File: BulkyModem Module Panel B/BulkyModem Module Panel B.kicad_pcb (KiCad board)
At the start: 2 copper layers, 100 x 23.2 mm, 20 parts, among them J1 Front Panel, M1 Mounting_Pin, M2 Mounting_Pin, M3 Mounting_Pin, M4 Mounting_Pin, SW1 MODE, SW2 POW

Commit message: Alternate panel designs
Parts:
- removed JP1: BYPASS, solder_bridge:bridge
- added R2: 2k2, Resistor_THT:R_Axial_DIN0207_L6.3mm_D2.5mm_P10.16mm_Horizontal, F.Cu at (132.2, 115.2)
- D17: value POW -> LED_RGBC; footprint LED_THT:LED_D5.0mm -> LED_THT:LED_D5.0mm-4_RGB_Wide_Pins
- R1: value 470 -> 3k3
- moved R1 38.7 mm to (117.6, 115.2)
- moved D4 19.7 mm to (148.7, 115.2), turned to 0 degrees
- moved D3 11.4 mm to (144.3, 115.2), turned to 180 degrees
- moved D17 3.32 mm to (96.7, 122.6), turned to 0 degrees
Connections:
- D17 pad 1: /LED_POW -> Net-(D17-Pad1)
- D3 pad 1: Net-(D17-Pad2) -> Net-(D3-Pad1)
- D4 pad 1: Net-(D17-Pad2) -> Net-(D3-Pad1)
- D4 pad 2: Net-(D4-Pad2) -> VSB
- J1 pad 3: /LED_POW -> (no net)
- R1 pad 1: VSB -> Net-(D3-Pad1)
- R1 pad 2: Net-(D4-Pad2) -> Net-(D17-Pad1)
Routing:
- net Net-(D3-Pad1): track 0.00 -> 35.2 mm
- net Net-(D4-Pad2): track 26.1 -> 0.00 mm
- net /LED_POW: track 24.8 -> 0.00 mm
- net VSB: track 24.8 -> 48.0 mm
- net Net-(D17-Pad1): track 0.00 -> 17.0 mm
- net Net-(D17-Pad2): track 41.6 -> 29.2 mm
- net VCC: track 119.8 -> 125.6 mm, vias 1 -> 0
- net /LED_C64: track 20.4 -> 18.8 mm
- net SW_PWR: track 23.0 -> 23.5 mm
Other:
- board text added: "BulkyModem Module Panel B (rev. A) github.com/tebl"
- board text removed: "BulkyModem Module Panel (rev. B) github.com/tebl"

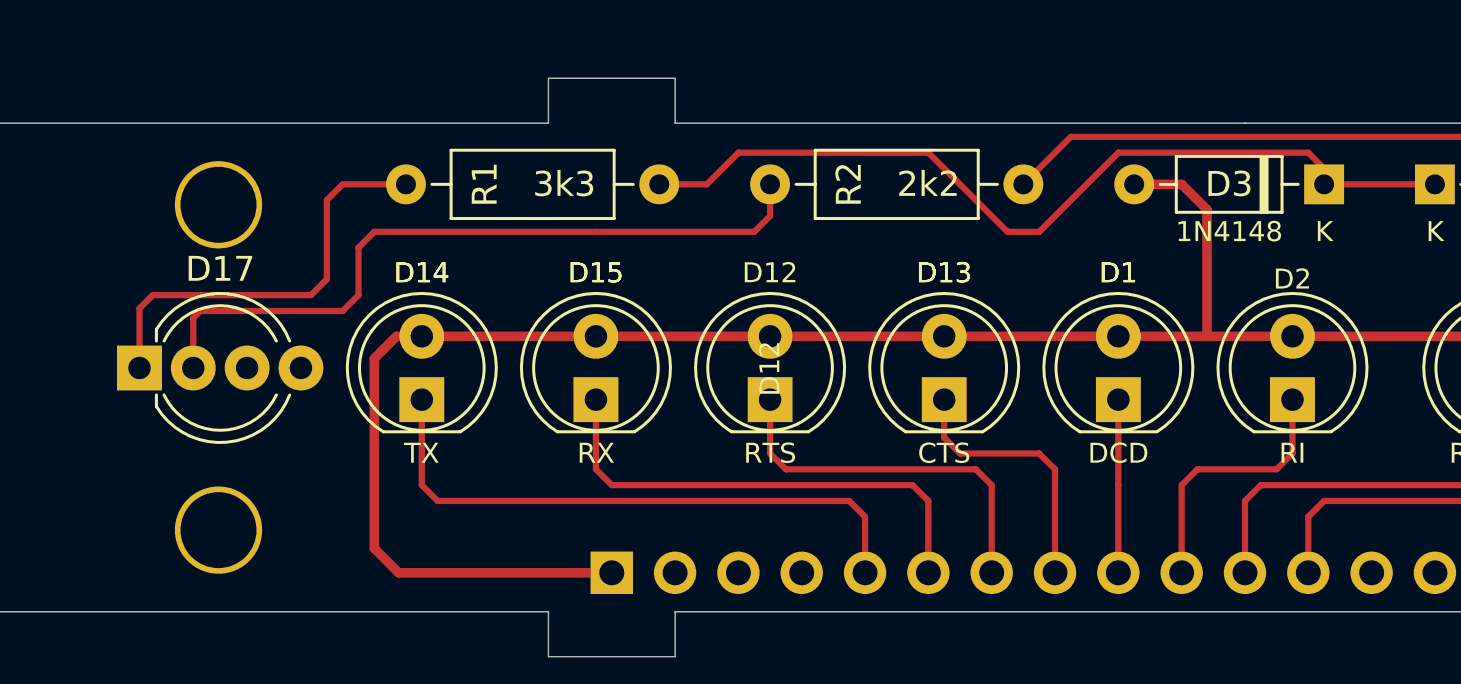
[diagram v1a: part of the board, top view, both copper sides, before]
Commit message: Tweaks needed to make revision C actually work.
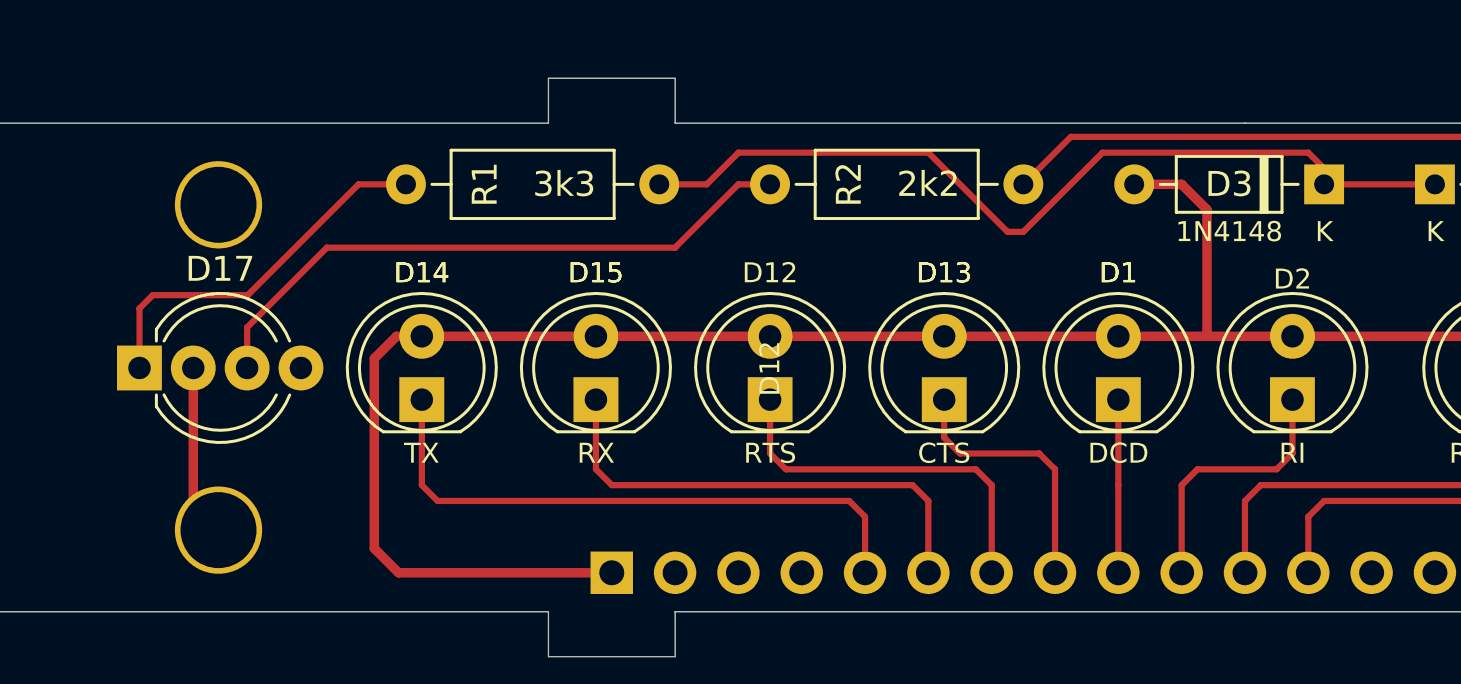
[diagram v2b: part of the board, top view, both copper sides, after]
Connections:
- D17 pad 2: Net-(D17-Pad2) -> GND
- D17 pad 3: (no net) -> Net-(D17-Pad3)
- D17 pad 4: GND -> (no net)
- R2 pad 2: Net-(D17-Pad2) -> Net-(D17-Pad3)
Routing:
- net Net-(D17-Pad2): track 29.2 -> 0.00 mm
- net Net-(D17-Pad3): track 0.00 -> 25.0 mm
- net GND: track 0.00 -> 6.92 mm
- net Net-(D17-Pad1): track 17.0 -> 15.1 mm
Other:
- board text added: "BulkyModem Module Panel B (rev. B) github.com/tebl"
- board text removed: "BulkyModem Module Panel B (rev. A) github.com/tebl"

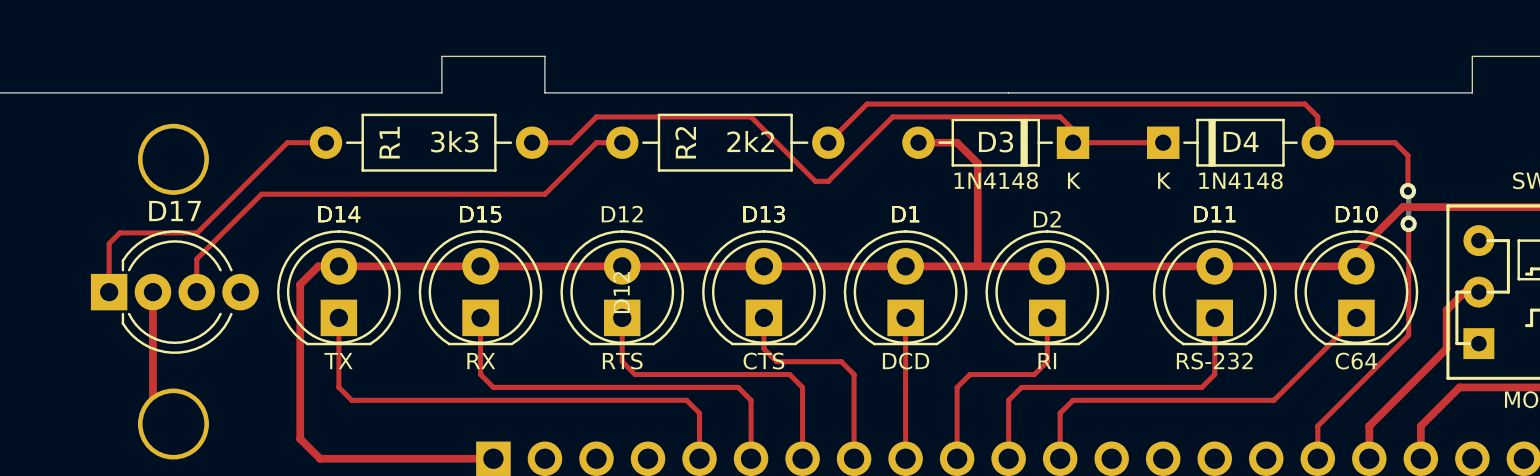
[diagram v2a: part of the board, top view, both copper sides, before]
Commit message: Change some resistor values
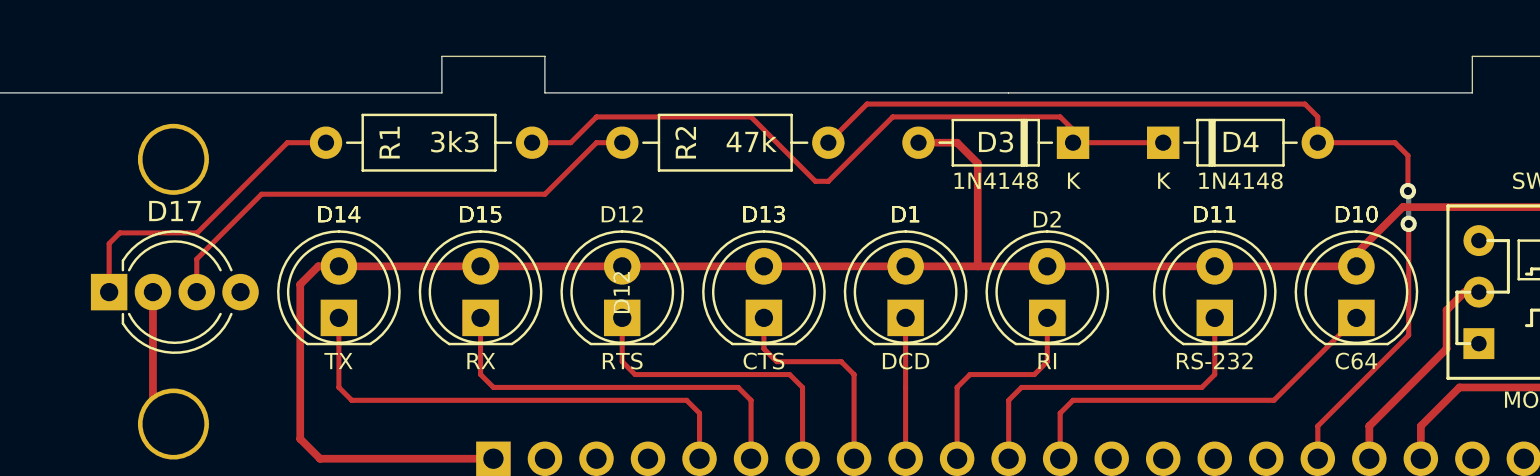
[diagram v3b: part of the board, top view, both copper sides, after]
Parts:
- R2: value 2k2 -> 47k
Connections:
- net /LED_C64 renamed /LED.C64
- net /LED_CTS renamed /LED.CTS
- net /LED_DCD renamed /LED.DCD
- net /LED_RI renamed /LED.RI
- net /LED_RS232 renamed /LED.RS232
- net /LED_RTS renamed /LED.RTS
- net /LED_RX renamed /LED.RX
- net /LED_TX renamed /LED.TX
- D17 pad 4: (no net) -> unconnected-(D17-BA-Pad4)
- J1 pad 13: (no net) -> unconnected-(J1-N.C.-Pad13)
- J1 pad 14: (no net) -> unconnected-(J1-N.C.-Pad14)
- J1 pad 15: (no net) -> unconnected-(J1-N.C.-Pad15)
- J1 pad 16: (no net) -> unconnected-(J1-N.C.-Pad16)
- J1 pad 3: (no net) -> unconnected-(J1-POW-Pad3)
- J1 pad 4: (no net) -> unconnected-(J1-STB-Pad4)
- SW1 pad 1: (no net) -> unconnected-(SW1A-A-Pad1)
- SW1 pad 4: (no net) -> unconnected-(SW1B-A-Pad4)
- SW1 pad 5: (no net) -> unconnected-(SW1B-B-Pad5)
- SW1 pad 6: (no net) -> unconnected-(SW1B-C-Pad6)
- SW2 pad 1: (no net) -> unconnected-(SW2A-A-Pad1)
- SW2 pad 4: (no net) -> unconnected-(SW2B-A-Pad4)
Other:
- net class Default removed
- net class PWR removed
